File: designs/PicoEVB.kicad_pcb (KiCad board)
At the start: 4 copper layers, 34.3 x 8.4 mm, 109 parts, among them J1 Bus_PCI_Express_x4, J10 1P2, J11 1P0, J12 GND, J2 2.54mm Through-Hole Socket, J3 2.54mm Through-Hole Socket, J7 3P3, J8 1P8, J9 1P0, P2 USB_C_Plug_USB2.0, U1A1 XC7AxxT-xCSG325, U2 S25Q, U3 TPS82085SIL, U4 MAX1589AETT100T, U5 MIC47050-1.2YML, U6 TPS82085SIL, U7 FT230XQ

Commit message: Add files via upload
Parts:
- C1, C10, C11, C12, C13, C14, C15, C16, C17, C18, C19, C2, C20, C21, C22, C23, C24, C25, C26, C3, C4, C5, C52, C53, C54, C55, C56, C57, C58, C59, C6, C60, C61, C62, C63, C64, C65, C66, C7, C8, C9, J10, J11, J12, J7, J8, J9, L1, R2, R3, R4, R5, U3, U4, U5, U6: moved to B.Cu
- moved C8 74.5 mm to (217.0, 102.0), turned to -90 degrees
- moved C5 74.5 mm to (216.0, 102.0), turned to -90 degrees
- moved C15 74.0 mm to (218.0, 102.0), turned to -90 degrees
- moved J11 72.9 mm to (216.0, 98.5), turned to -90 degrees
- moved C1 72.7 mm to (211.5, 106.0), turned to 90 degrees
- moved C7 71.9 mm to (221.5, 99.7), turned to 90 degrees
- moved J12 71.8 mm to (216.0, 109.5), turned to 90 degrees
- moved J7 71.6 mm to (216.0, 105.0), turned to 90 degrees
- moved C12 71.1 mm to (222.0, 99.7), turned to 90 degrees
- moved C17 70.4 mm to (222.5, 99.7), turned to 90 degrees
- moved C3 68.4 mm to (220.0, 98.5), turned to 90 degrees
- moved C26 68.1 mm to (221.5, 101.5), turned to -90 degrees
- moved C18 67.9 mm to (219.0, 101.5), turned to -90 degrees
- moved C55 67.5 mm to (216.1, 115.0), turned to -90 degrees
- moved C20 67.4 mm to (219.5, 101.5), turned to -90 degrees
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- renumbered U1A1 to U1
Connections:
- C52 pad 1: VCC_BANK14_B -> +3V3
- C53 pad 1: VCC_BANK14_B -> +3V3
- C54 pad 1: VCC_BANK14_B -> +3V3
- C55 pad 1: VCC_BANK14_B -> +3V3
- C58 pad 1: VCC_BANK14_B -> +3V3
- C59 pad 1: VCC_BANK14_B -> +3V3
- C67 pad 1: VCC_BANK14_B -> +3V3
- C68 pad 1: VCC_BANK14_B -> +3V3
- C69 pad 1: VCC_BANK14_B -> +3V3
- C70 pad 2: VCC_BANK14_B -> +3V3
- J1 pad A10: VCC_BANK14_B -> +3V3
- J1 pad A2: unconnected-(J1-+12V-PadA2)_4 -> +3V3
- J1 pad A3: unconnected-(J1-+12V-PadA2)_2 -> +3V3
- J1 pad A9: VCC_BANK14_B -> +3V3
- J1 pad B1: unconnected-(J1-+12V-PadA2)_3 -> +3V3
- J1 pad B10: unconnected-(J1-3.3Vaux-PadB10) -> +3V3
- J1 pad B2: unconnected-(J1-+12V-PadA2) -> +3V3
- J1 pad B3: unconnected-(J1-+12V-PadA2)_1 -> +3V3
- J1 pad B8: VCC_BANK14_B -> +3V3
- J2 pad 1: VCC_BANK14_B -> +3V3
- J2 pad 39: VCC_BANK14_B -> +3V3
- J3 pad 1: VCC_BANK14_B -> +3V3
- J3 pad 39: VCC_BANK14_B -> +3V3
- J7 pad 1: VCC_BANK14_B -> +3V3
- R1 pad 1: Net-(U1E1E-MGTRREF_216) -> Net-(U1E-MGTRREF_216)
- U1 pad A1: (no net) -> GND
- U1 pad A10: (no net) -> XADC_2_N
- U1 pad A11: (no net) -> GND
- U1 pad A12: (no net) -> XADC_3_N
- U1 pad A13: (no net) -> unconnected-(U1C-IO_L8P_T1_AD10P_15-PadA13)
- U1 pad A14: (no net) -> unconnected-(U1C-IO_L8N_T1_AD10N_15-PadA14)
- U1 pad A15: (no net) -> unconnected-(U1C-IO_L10N_T1_AD11N_15-PadA15)
- U1 pad A16: (no net) -> VCC_BANK14_B
- U1 pad A17: (no net) -> unconnected-(U1C-IO_L15N_T2_DQS_ADV_B_15-PadA17)
- U1 pad A18: (no net) -> GND
- U1 pad A2: (no net) -> P1V2_MGTAVTT_B
- U1 pad A3: (no net) -> GND
- U1 pad A4: (no net) -> GND
- U1 pad A5: (no net) -> GND
- U1 pad A6: (no net) -> Net-(U1E-MGTRREF_216)
- U1 pad A7: (no net) -> GND
- U1 pad A8: (no net) -> GND
- U1 pad A9: (no net) -> unconnected-(U1C-IO_L3N_T0_DQS_AD1N_15-PadA9)
- U1 pad B1: (no net) -> MGT0_TX_B-
- U1 pad B10: (no net) -> XADC_2_P
- U1 pad B11: (no net) -> DIO_0_N
- U1 pad B12: (no net) -> XADC_3_P
- U1 pad B13: (no net) -> VCC_BANK14_B
- U1 pad B14: (no net) -> unconnected-(U1C-IO_L10P_T1_AD11P_15-PadB14)
- U1 pad B15: (no net) -> unconnected-(U1C-IO_L9N_T1_DQS_AD3N_15-PadB15)
- U1 pad B16: (no net) -> unconnected-(U1C-IO_L15P_T2_DQS_15-PadB16)
- U1 pad B17: (no net) -> DIO_1_N
- U1 pad B18: (no net) -> GND
- U1 pad B2: (no net) -> MGT0_TX_B+
- U1 pad B3: (no net) -> GND
- U1 pad B4: (no net) -> P1V0_MGTAVCC_B
- U1 pad B5: (no net) -> MGT_REFCLK0_B-
- U1 pad B6: (no net) -> MGT_REFCLK0_B+
- U1 pad B7: (no net) -> GND
- U1 pad B8: (no net) -> GND
- U1 pad B9: (no net) -> unconnected-(U1C-IO_L3P_T0_DQS_AD1P_15-PadB9)
- U1 pad C1: (no net) -> P1V2_MGTAVTT_B
- U1 pad C10: (no net) -> VCC_BANK14_B
- U1 pad C11: (no net) -> DIO_0_P
- U1 pad C12: (no net) -> unconnected-(U1C-IO_L6N_T0_VREF_15-PadC12)
- U1 pad C13: (no net) -> unconnected-(U1C-IO_L11N_T1_SRCC_15-PadC13)
- U1 pad C14: (no net) -> unconnected-(U1C-IO_L9P_T1_DQS_AD3P_15-PadC14)
- U1 pad C15: (no net) -> GND
- U1 pad C16: (no net) -> DIO_1_P
- U1 pad C17: (no net) -> DIO_3_P
- U1 pad C18: (no net) -> DIO_3_N
- U1 pad C2: (no net) -> GND
- U1 pad C3: (no net) -> Net-(U1E-MGTPRXN2_216)
- U1 pad C4: (no net) -> Net-(U1E-MGTPRXP2_216)
- U1 pad C5: (no net) -> P1V0_MGTAVCC_B
- U1 pad C6: (no net) -> GND
- U1 pad C7: (no net) -> GND
- U1 pad C8: (no net) -> XADC_0_N
- U1 pad C9: (no net) -> XADC_1_N
- U1 pad D1: (no net) -> Net-(U1E-MGTPRXN2_216)
- U1 pad D10: (no net) -> GPIO_0
- U1 pad D11: (no net) -> unconnected-(U1C-IO_L6P_T0_15-PadD11)
- U1 pad D12: (no net) -> GND
- U1 pad D13: (no net) -> unconnected-(U1C-IO_L11P_T1_SRCC_15-PadD13)
- U1 pad D14: (no net) -> MRCC_Out_1
- U1 pad D15: (no net) -> MRCC_Out_3
- U1 pad D16: (no net) -> unconnected-(U1C-IO_L14N_T2_SRCC_15-PadD16)
- U1 pad D17: (no net) -> VCC_BANK14_B
- U1 pad D18: (no net) -> DIO_2_N
- U1 pad D2: (no net) -> Net-(U1E-MGTPRXP2_216)
- U1 pad D3: (no net) -> GND
- U1 pad D4: (no net) -> GND
- U1 pad D5: (no net) -> /FPGA PCIe/UMGTCLK_0-
- U1 pad D6: (no net) -> /FPGA PCIe/UMGTCLK_0+
- U1 pad D7: (no net) -> GND
- U1 pad D8: (no net) -> XADC_0_P
- U1 pad D9: (no net) -> XADC_1_P
- U1 pad E1: (no net) -> P1V2_MGTAVTT_B
- U1 pad E13: (no net) -> MRCC_Out_0
- U1 pad E14: (no net) -> VCC_BANK14_B
- U1 pad E15: (no net) -> MRCC_Out_2
- U1 pad E16: (no net) -> unconnected-(U1C-IO_L14P_T2_SRCC_15-PadE16)
- U1 pad E17: (no net) -> DIO_2_P
- U1 pad E18: (no net) -> DIO_7_N
- U1 pad E2: (no net) -> GND
- U1 pad E3: (no net) -> MGT1_RX_B-
- U1 pad E4: (no net) -> MGT1_RX_B+
- U1 pad E5: (no net) -> P1V0_MGTAVCC_B
- U1 pad E6: (no net) -> GND
- U1 pad E7: (no net) -> GND
- U1 pad E9: (no net) -> GND
- U1 pad F1: (no net) -> unconnected-(U1E-MGTPTXN1_216-PadF1)
- U1 pad F10: (no net) -> GND
- U1 pad F11: (no net) -> P1V0_VCC_FPGA_B
- U1 pad F14: (no net) -> DIO_5_N
- U1 pad F15: (no net) -> unconnected-(U1C-IO_L21N_T3_DQS_A18_15-PadF15)
- U1 pad F16: (no net) -> GND
- U1 pad F17: (no net) -> DIO_7_P
- U1 pad F18: (no net) -> unconnected-(U1C-IO_L19N_T3_A21_VREF_15-PadF18)
- U1 pad F2: (no net) -> unconnected-(U1E-MGTPTXP1_216-PadF2)
- U1 pad F3: (no net) -> P1V2_MGTAVTT_B
- U1 pad F4: (no net) -> GND
- U1 pad F5: (no net) -> P1V0_MGTAVCC_B
- U1 pad F6: (no net) -> GND
- U1 pad F7: (no net) -> P1V0_VCC_FPGA_B
- U1 pad F9: (no net) -> P1V0_VCC_FPGA_B
- U1 pad G1: (no net) -> GND
- U1 pad G10: (no net) -> P1V0_VCC_FPGA_B
- U1 pad G11: (no net) -> GND
- U1 pad G12: (no net) -> P1V8_FPGA_VCCAUX_B
- U1 pad G13: (no net) -> GND
- U1 pad G14: (no net) -> DIO_5_P
- U1 pad G15: (no net) -> unconnected-(U1C-IO_L21P_T3_DQS_15-PadG15)
- U1 pad G16: (no net) -> DIO_4_N
- U1 pad G17: (no net) -> unconnected-(U1C-IO_L19P_T3_A22_15-PadG17)
- U1 pad G18: (no net) -> VCC_BANK14_B
- U1 pad G2: (no net) -> P1V2_MGTAVTT_B
- U1 pad G3: (no net) -> MGT0_RX_B-
- U1 pad G4: (no net) -> MGT0_RX_B+
- U1 pad G5: (no net) -> GND
- U1 pad G6: (no net) -> GND
- U1 pad G7: (no net) -> GND
- U1 pad G8: (no net) -> P1V0_VCC_FPGA_B
- U1 pad G9: (no net) -> GND
- U1 pad H1: (no net) -> MGT1_TX_B-
- U1 pad H10: (no net) -> GND
- U1 pad H11: (no net) -> P1V0_VCC_FPGA_B
- U1 pad H12: (no net) -> GND
- U1 pad H13: (no net) -> P1V8_FPGA_VCCAUX_B
- U1 pad H14: (no net) -> GPIO_1
- U1 pad H15: (no net) -> VCC_BANK14_B
- U1 pad H16: (no net) -> DIO_4_P
- U1 pad H17: (no net) -> DIO_6_P
- U1 pad H18: (no net) -> DIO_6_N
- U1 pad H2: (no net) -> MGT1_TX_B+
- U1 pad H3: (no net) -> GND
- U1 pad H4: (no net) -> GND
- U1 pad H5: (no net) -> GND
- U1 pad H6: (no net) -> GND
- U1 pad H7: (no net) -> P1V0_VCC_FPGA_B
- U1 pad H8: (no net) -> GND
- U1 pad H9: (no net) -> P1V0_VCC_FPGA_B
- U1 pad J1: (no net) -> GND
- U1 pad J11: (no net) -> GND
- U1 pad J12: (no net) -> P1V0_VCC_FPGA_B
- U1 pad J13: (no net) -> GND
- U1 pad J14: (no net) -> unconnected-(U1B-IO_L5P_T0_D06_14-PadJ14)
- U1 pad J15: (no net) -> Net-(RN3-R3.2)
- U1 pad J16: (no net) -> Net-(RN3-R2.2)
- U1 pad J17: (no net) -> GND
- U1 pad J18: (no net) -> VCC_BANK14_B
- U1 pad J2: (no net) -> GND
- U1 pad J3: (no net) -> GND
- U1 pad J4: (no net) -> DIO_9_N
- U1 pad J5: (no net) -> DIO_9_P
- U1 pad J6: (no net) -> GPIO_2
- U1 pad J7: (no net) -> GND
- U1 pad J8: (no net) -> P1V0_VCC_FPGA_B
- U1 pad K1: (no net) -> unconnected-(U1D-IO_L3N_T0_DQS_34-PadK1)
- U1 pad K11: (no net) -> P1V0_VCC_FPGA_B
- U1 pad K12: (no net) -> GND
- U1 pad K13: (no net) -> P1V8_FPGA_VCCAUX_B
- U1 pad K14: (no net) -> GND
- U1 pad K15: (no net) -> unconnected-(U1B-IO_L5N_T0_D07_14-PadK15)
- U1 pad K16: (no net) -> Net-(U1B-IO_L1P_T0_D00_MOSI_14)
- U1 pad K17: (no net) -> unconnected-(U1B-IO_L4P_T0_D04_14-PadK17)
- U1 pad K18: (no net) -> unconnected-(U1B-IO_L3N_T0_DQS_EMCCLK_14-PadK18)
- U1 pad K2: (no net) -> unconnected-(U1D-IO_L3P_T0_DQS_34-PadK2)
- U1 pad K3: (no net) -> DIO_10_P
- U1 pad K4: (no net) -> GND
- U1 pad K5: (no net) -> DIO_8_N
- U1 pad K6: (no net) -> DIO_8_P
- U1 pad K7: (no net) -> P1V0_VCC_FPGA_B
- U1 pad K8: (no net) -> GND
- U1 pad L1: (no net) -> GND
- U1 pad L11: (no net) -> GND
- U1 pad L12: (no net) -> P1V0_VCC_FPGA_B
- U1 pad L13: (no net) -> GND
- U1 pad L14: (no net) -> GPIO_4
- U1 pad L15: (no net) -> Net-(RN3-R4.2)
- U1 pad L16: (no net) -> VCC_BANK14_B
- U1 pad L17: (no net) -> Net-(U1B-IO_L1N_T0_D01_DIN_14)
- U1 pad L18: (no net) -> unconnected-(U1B-IO_L4N_T0_D05_14-PadL18)
- U1 pad L2: (no net) -> DIO_10_N
- U1 pad L3: (no net) -> DIO_11_N
- U1 pad L4: (no net) -> DIO_11_P
- U1 pad L5: (no net) -> unconnected-(U1D-IO_L6P_T0_34-PadL5)
- U1 pad L6: (no net) -> VCC_BANK14_B
- U1 pad L7: (no net) -> GND
- U1 pad L8: (no net) -> P1V0_VCC_FPGA_B
- U1 pad M1: (no net) -> DIO_12_N
- U1 pad M11: (no net) -> P1V0_VCC_FPGA_B
- U1 pad M12: (no net) -> GND
- U1 pad M13: (no net) -> P1V8_FPGA_VCCAUX_B
- U1 pad M14: (no net) -> unconnected-(U1B-IO_L8P_T1_D11_14-PadM14)
- U1 pad M15: (no net) -> unconnected-(U1B-IO_L6N_T0_D08_VREF_14-PadM15)
- U1 pad M16: (no net) -> unconnected-(U1B-IO_L7P_T1_D09_14-PadM16)
- U1 pad M17: (no net) -> unconnected-(U1B-IO_L7N_T1_D10_14-PadM17)
- U1 pad M18: (no net) -> GND
- U1 pad M2: (no net) -> DIO_12_P
- U1 pad M3: (no net) -> VCC_BANK14_B
- U1 pad M4: (no net) -> DIO_14_P
- U1 pad M5: (no net) -> unconnected-(U1D-IO_L6N_T0_VREF_34-PadM5)
- U1 pad M6: (no net) -> DIO_13_P
- U1 pad M7: (no net) -> P1V0_VCC_FPGA_B
- U1 pad M8: (no net) -> GND
- U1 pad N1: (no net) -> unconnected-(U1D-IO_L9P_T1_DQS_34-PadN1)
- U1 pad N10: (no net) -> P1V0_VCC_FPGA_B
- U1 pad N11: (no net) -> GND
- U1 pad N12: (no net) -> P1V0_VCC_FPGA_B
- U1 pad N13: (no net) -> GND
- U1 pad N14: (no net) -> unconnected-(U1B-IO_L8N_T1_D12_14-PadN14)
- U1 pad N15: (no net) -> GND
- U1 pad N16: (no net) -> unconnected-(U1B-IO_L9P_T1_DQS_14-PadN16)
- U1 pad N17: (no net) -> unconnected-(U1B-IO_L9N_T1_DQS_D13_14-PadN17)
- U1 pad N18: (no net) -> unconnected-(U1B-IO_L10P_T1_D14_14-PadN18)
- U1 pad N2: (no net) -> unconnected-(U1D-IO_L11N_T1_SRCC_34-PadN2)
- U1 pad N3: (no net) -> unconnected-(U1D-IO_L11P_T1_SRCC_34-PadN3)
- U1 pad N4: (no net) -> DIO_14_N
- U1 pad N5: (no net) -> GND
- U1 pad N6: (no net) -> DIO_13_N
- U1 pad N7: (no net) -> GND
- U1 pad N8: (no net) -> P1V0_VCC_FPGA_B
- U1 pad N9: (no net) -> GND
- U1 pad P1: (no net) -> unconnected-(U1D-IO_L9N_T1_DQS_34-PadP1)
- U1 pad P11: (no net) -> P1V0_VCC_FPGA_B
- U1 pad P12: (no net) -> GND
- U1 pad P13: (no net) -> P1V8_FPGA_VCCAUX_B
- U1 pad P14: (no net) -> unconnected-(U1B-IO_L12P_T1_MRCC_14-PadP14)
- U1 pad P15: (no net) -> unconnected-(U1B-IO_L11P_T1_SRCC_14-PadP15)
- U1 pad P16: (no net) -> unconnected-(U1B-IO_L11N_T1_SRCC_14-PadP16)
- U1 pad P17: (no net) -> VCC_BANK14_B
- U1 pad P18: (no net) -> unconnected-(U1B-IO_L10N_T1_D15_14-PadP18)
- U1 pad P2: (no net) -> GND
- U1 pad P3: (no net) -> unconnected-(U1D-IO_L12N_T1_MRCC_34-PadP3)
- U1 pad P4: (no net) -> unconnected-(U1D-IO_L12P_T1_MRCC_34-PadP4)
- U1 pad P5: (no net) -> unconnected-(U1D-IO_L19N_T3_VREF_34-PadP5)
- U1 pad P6: (no net) -> unconnected-(U1D-IO_L19P_T3_34-PadP6)
- U1 pad P7: (no net) -> VCC_BANK14_B
- U1 pad P8: (no net) -> GND
- U1 pad P9: (no net) -> P1V0_VCC_FPGA_B
- U1 pad R1: (no net) -> unconnected-(U1D-IO_L13N_T2_MRCC_34-PadR1)
- U1 pad R13: (no net) -> unconnected-(U1B-IO_L19P_T3_A10_D26_14-PadR13)
- U1 pad R14: (no net) -> VCC_BANK14_B
- U1 pad R15: (no net) -> unconnected-(U1B-IO_L12N_T1_MRCC_14-PadR15)
- U1 pad R16: (no net) -> unconnected-(U1B-IO_L14P_T2_SRCC_14-PadR16)
- U1 pad R17: (no net) -> unconnected-(U1B-IO_L14N_T2_SRCC_14-PadR17)
- U1 pad R18: (no net) -> unconnected-(U1B-IO_L15P_T2_DQS_RDWR_B_14-PadR18)
- U1 pad R2: (no net) -> unconnected-(U1D-IO_L13P_T2_MRCC_34-PadR2)
- U1 pad R3: (no net) -> unconnected-(U1D-IO_L14P_T2_SRCC_34-PadR3)
- U1 pad R4: (no net) -> VCC_BANK14_B
- U1 pad R5: (no net) -> unconnected-(U1D-IO_L21P_T3_DQS_34-PadR5)
- U1 pad R6: (no net) -> GPIO_3
- U1 pad R7: (no net) -> unconnected-(U1D-IO_L22P_T3_34-PadR7)
- U1 pad R9: (no net) -> GND
- U1 pad T1: (no net) -> VCC_BANK14_B
- U1 pad T11: (no net) -> VCC_BANK14_B
- U1 pad T12: (no net) -> unconnected-(U1B-IO_L22P_T3_A05_D21_14-PadT12)
- U1 pad T13: (no net) -> unconnected-(U1B-IO_L19N_T3_A09_D25_VREF_14-PadT13)
- U1 pad T14: (no net) -> unconnected-(U1B-IO_L13P_T2_MRCC_14-PadT14)
- U1 pad T15: (no net) -> unconnected-(U1B-IO_L13N_T2_MRCC_14-PadT15)
- U1 pad T16: (no net) -> GND
- U1 pad T17: (no net) -> unconnected-(U1B-IO_L16P_T2_CSI_B_14-PadT17)
- U1 pad T18: (no net) -> unconnected-(U1B-IO_L15N_T2_DQS_DOUT_CSO_B_14-PadT18)
- U1 pad T2: (no net) -> unconnected-(U1D-IO_L14N_T2_SRCC_34-PadT2)
- U1 pad T3: (no net) -> DIO_15_N
- U1 pad T4: (no net) -> DIO_15_P
- U1 pad T5: (no net) -> unconnected-(U1D-IO_L21N_T3_DQS_34-PadT5)
- U1 pad T6: (no net) -> GND
- U1 pad T7: (no net) -> unconnected-(U1D-IO_L22N_T3_34-PadT7)
- U1 pad U1: (no net) -> unconnected-(U1D-IO_L15N_T2_DQS_34-PadU1)
- U1 pad U10: (no net) -> GPIO_5
- U1 pad U11: (no net) -> unconnected-(U1B-IO_L23P_T3_A03_D19_14-PadU11)
- U1 pad U12: (no net) -> unconnected-(U1B-IO_L22N_T3_A04_D20_14-PadU12)
- U1 pad U13: (no net) -> GND
- U1 pad U14: (no net) -> unconnected-(U1B-IO_L20P_T3_A08_D24_14-PadU14)
- U1 pad U15: (no net) -> unconnected-(U1B-IO_L17P_T2_A14_D30_14-PadU15)
- U1 pad U16: (no net) -> unconnected-(U1B-IO_L17N_T2_A13_D29_14-PadU16)
- U1 pad U17: (no net) -> unconnected-(U1B-IO_L16N_T2_A15_D31_14-PadU17)
- U1 pad U18: (no net) -> VCC_BANK14_B
- U1 pad U2: (no net) -> unconnected-(U1D-IO_L15P_T2_DQS_34-PadU2)
- U1 pad U3: (no net) -> GND
- U1 pad U4: (no net) -> DIO_16_P
- U1 pad U5: (no net) -> unconnected-(U1D-IO_L20N_T3_34-PadU5)
- U1 pad U6: (no net) -> unconnected-(U1D-IO_L20P_T3_34-PadU6)
- U1 pad U7: (no net) -> unconnected-(U1D-IO_L23P_T3_34-PadU7)
- U1 pad U8: (no net) -> VCC_BANK14_B
- U1 pad U9: (no net) -> unconnected-(U1B-IO_L24P_T3_A01_D17_14-PadU9)
- U1 pad V1: (no net) -> GND
- U1 pad V10: (no net) -> GND
- U1 pad V11: (no net) -> unconnected-(U1B-IO_L23N_T3_A02_D18_14-PadV11)
- U1 pad V12: (no net) -> Net-(D3-K)
- U1 pad V13: (no net) -> Net-(D4-K)
- U1 pad V14: (no net) -> Net-(D2-K)
- U1 pad V15: (no net) -> VCC_BANK14_B
- U1 pad V16: (no net) -> unconnected-(U1B-IO_L18P_T2_A12_D28_14-PadV16)
- U1 pad V17: (no net) -> unconnected-(U1B-IO_L18N_T2_A11_D27_14-PadV17)
- U1 pad V18: (no net) -> GND
- U1 pad V2: (no net) -> M2_LED_1
- U1 pad V3: (no net) -> M2_LED_2
- U1 pad V4: (no net) -> DIO_16_N
- U1 pad V5: (no net) -> VCC_BANK14_B
- U1 pad V6: (no net) -> unconnected-(U1D-IO_L23N_T3_34-PadV6)
- U1 pad V7: (no net) -> unconnected-(U1D-IO_L24N_T3_34-PadV7)
- U1 pad V8: (no net) -> unconnected-(U1D-IO_L24P_T3_34-PadV8)
- U1 pad V9: (no net) -> unconnected-(U1B-IO_L24N_T3_A00_D16_14-PadV9)
- U2 pad 2: Net-(U1B1B-IO_L1N_T0_D01_DIN_14) -> Net-(U1B-IO_L1N_T0_D01_DIN_14)
- U2 pad 5: Net-(U1B1B-IO_L1P_T0_D00_MOSI_14) -> Net-(U1B-IO_L1P_T0_D00_MOSI_14)
- U3 pad 1: VCC_BANK14_B -> +3V3
- U3 pad 3: VCC_BANK14_B -> +3V3
- U3 pad 4: VCC_BANK14_B -> +3V3
- U5 pad 1: VCC_BANK14_B -> +3V3
- U5 pad 6: VCC_BANK14_B -> +3V3
- U6 pad 1: VCC_BANK14_B -> +3V3
- U6 pad 3: VCC_BANK14_B -> +3V3
- U6 pad 4: VCC_BANK14_B -> +3V3
- U7 pad 1: VCC_BANK14_B -> +3V3
- U7 pad 10: VCC_BANK14_B -> +3V3
- U7 pad 8: VCC_BANK14_B -> +3V3
- U7 pad 9: VCC_BANK14_B -> Net-(U7-~{RESET})
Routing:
- net GND: track 0.00 -> 128.5 mm, vias 0 -> 60
- net +3V3: track 0.00 -> 51.7 mm, vias 0 -> 17
- net P1V0_VCC_FPGA_B: track 0.00 -> 41.6 mm, vias 0 -> 1
- net P1V8_FPGA_VCCAUX_B: track 0.00 -> 22.4 mm
- net P1V2_MGTAVTT_B: track 0.00 -> 18.1 mm, vias 0 -> 1
- net Net-(U3-VOUT): track 0.00 -> 17.8 mm
- net P1V0_MGTAVCC_B: track 0.00 -> 16.8 mm, vias 0 -> 1
- net Net-(U6-FB): track 0.00 -> 2.71 mm
- net Net-(U3-FB): track 0.00 -> 1.55 mm
- added copper zone on In2.Cu, net +3V3
- added copper zone on In1.Cu, net GND
- added copper zone on In3.Cu, net GND
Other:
- copper layers 4 -> 6

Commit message: Add changes
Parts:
- added ?: , , F.Cu at (193.3, 66.7)
- added C13: 0.1uf, SMT:c_0201_least, B.Cu at (205.7, 55.2)
- added C14: 0.1uf, SMT:c_0201_least, B.Cu at (193.5, 67.3)
- added C14: 0.1uf, SMT:c_0201_least, B.Cu at (193.5, 67.8)
- added C14: 0.1uf, SMT:c_0201_least, B.Cu at (193.5, 66.7)
- added C18: 0.47uf, SMT:c_0201_least, B.Cu at (228.4, 67.6)
- added C18: 0.47uf, SMT:c_0201_least, B.Cu at (225.3, 67.6)
- added C20: 0.47uf, SMT:c_0201_least, B.Cu at (228.9, 67.6)
- added C20: 0.47uf, SMT:c_0201_least, B.Cu at (225.8, 67.6)
- added C21: 0.47uf, SMT:c_0201_least, B.Cu at (199.5, 62.4)
- added C22: 0.47uf, SMT:c_0201_least, B.Cu at (229.4, 67.6)
- added C22: 0.47uf, SMT:c_0201_least, B.Cu at (226.3, 67.6)
- added C23: 0.47uf, SMT:c_0201_least, B.Cu at (200.5, 62.4)
- added C24: 0.47uf, SMT:c_0201_least, B.Cu at (226.8, 67.6)
- added C25: 0.47uf, SMT:c_0201_least, B.Cu at (227.3, 67.6)
- added C26: 0.47uf, SMT:c_0201_least, B.Cu at (227.8, 67.6)
- added C9: 0.1uf, SMT:c_0201_least, B.Cu at (205.6, 56.0)
- moved C1 55.3 mm to (204.0, 51.2)
- moved C9 54.3 mm to (204.8, 52.4)
- moved C13 53.5 mm to (205.6, 53.2)
- moved C11 37.9 mm to (194.4, 62.1)
- moved C16 37.9 mm to (195.4, 62.4)
- moved C19 37.9 mm to (196.4, 62.4)
- moved C21 37.9 mm to (197.4, 62.4)
- moved C23 37.9 mm to (198.4, 62.4)
- moved C4 37.9 mm to (191.9, 61.9)
- moved C6 37.9 mm to (193.4, 62.1)
- moved C12 34.9 mm to (230.3, 65.8)
- moved C17 34.9 mm to (230.8, 65.8)
- moved C7 34.9 mm to (229.8, 65.8)
- moved C15 34.1 mm to (221.2, 68.1)
- moved C18 34.1 mm to (222.2, 67.6)
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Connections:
- U3 pad : (no net) -> GND
- U6 pad : (no net) -> GND
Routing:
- net GND: track 128.5 -> 107.0 mm, vias 60 -> 182
- net Net-(U3-VOUT): track 17.8 -> 6.30 mm
- net P1V0_VCC_FPGA_B: track 41.6 -> 51.8 mm, vias 1 -> 21
- net P1V2_MGTAVTT_B: track 18.1 -> 20.3 mm, vias 1 -> 5
- net P1V8_FPGA_VCCAUX_B: track 22.4 -> 23.7 mm, vias 0 -> 6
- net +3V3: track 51.7 -> 52.3 mm, vias 17 -> 16
- net Net-(U3-FB): track 1.55 -> 2.05 mm
- net P1V0_MGTAVCC_B: track 16.8 -> 16.4 mm, vias 1 -> 4
- net unconnected-(U1E-MGTPTXP1_216-PadF2): vias 0 -> 1
- net unconnected-(U1E-MGTPTXN1_216-PadF1): vias 0 -> 1
- net unconnected-(U1D-IO_L9P_T1_DQS_34-PadN1): vias 0 -> 1
- net unconnected-(U1D-IO_L9N_T1_DQS_34-PadP1): vias 0 -> 1
- net unconnected-(U1D-IO_L6P_T0_34-PadL5): vias 0 -> 1
- net unconnected-(U1D-IO_L6N_T0_VREF_34-PadM5): vias 0 -> 1
- net unconnected-(U1D-IO_L3P_T0_DQS_34-PadK2): vias 0 -> 1
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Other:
- board text added: "0.47uf"
- board text added: "Needs 21 decoupling caps in total, VCCBRAM only 3"
- board text added: "THESE 3 ARE FOR VCCBRAM: F11, G10, H11"

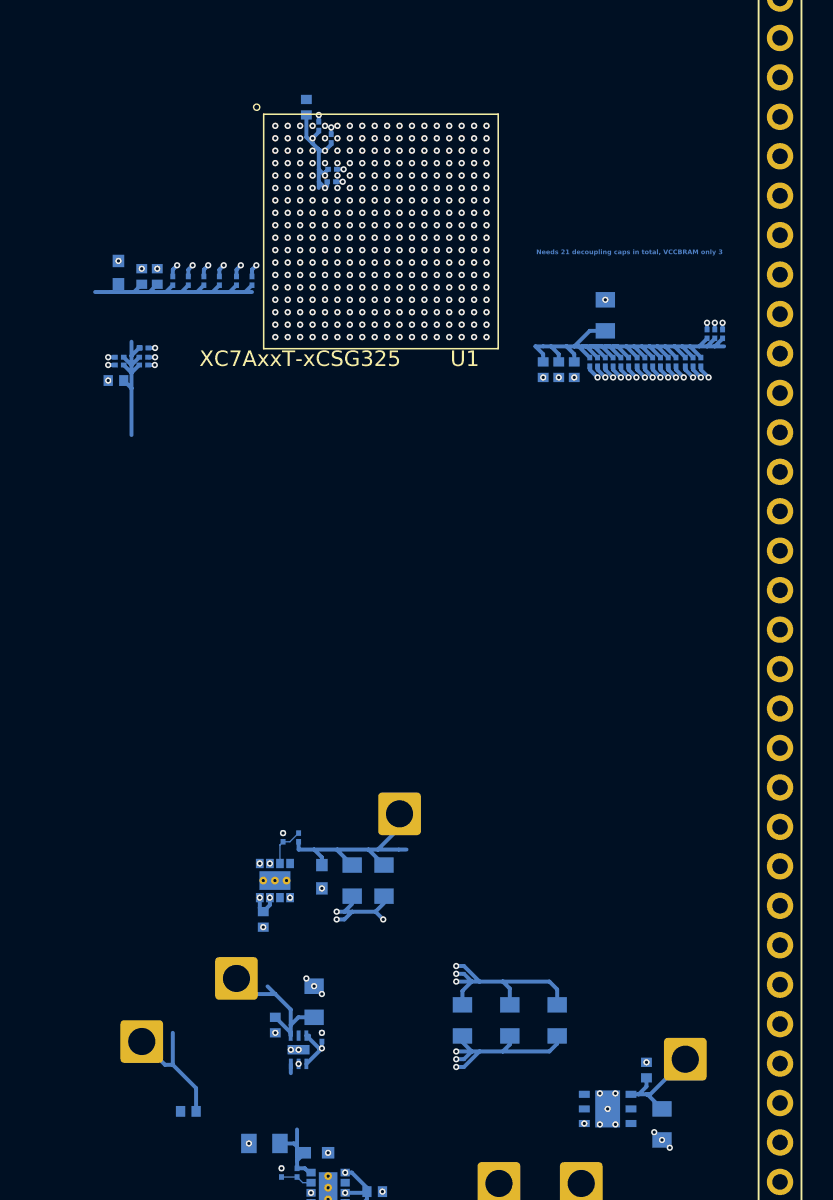
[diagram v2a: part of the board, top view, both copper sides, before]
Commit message: Commit power circuits for chip
All power circuits for chip are DONE. In progress: Connecting bottom of board power circuits.
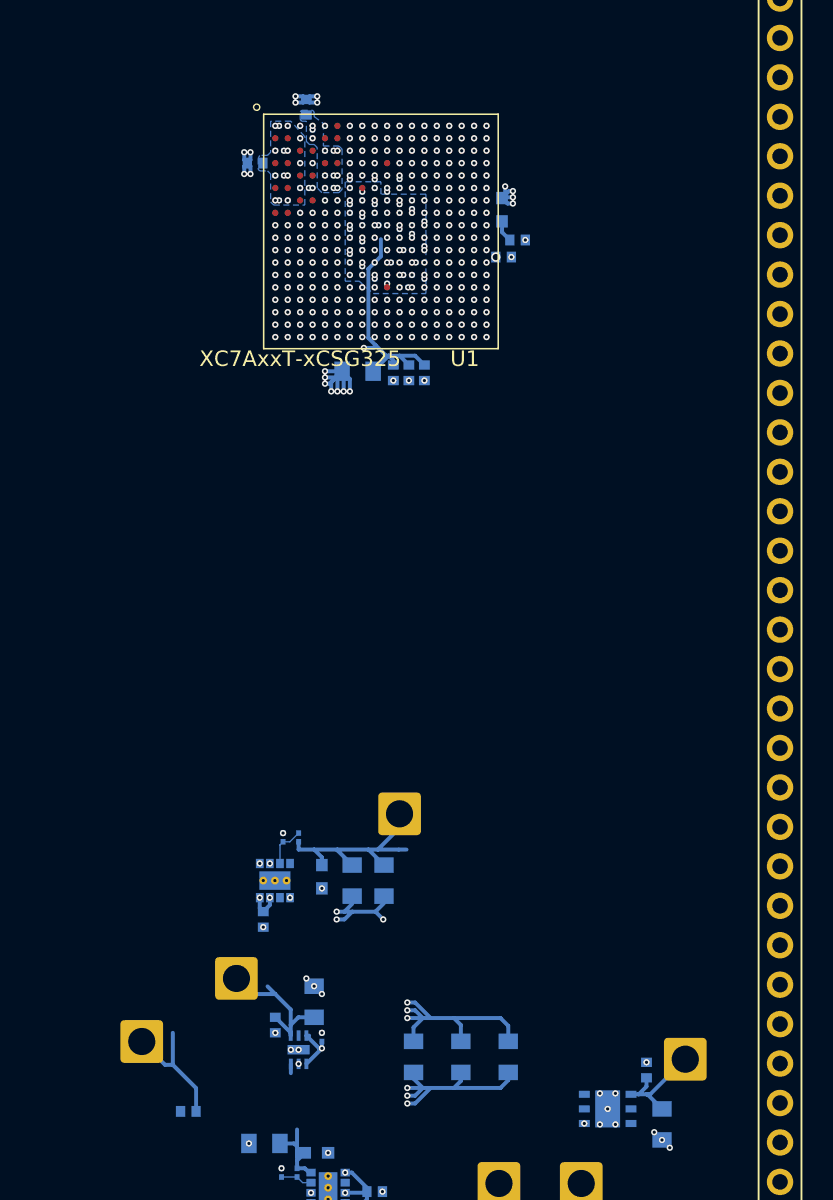
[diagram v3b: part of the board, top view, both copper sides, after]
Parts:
- added C18: 0.47uf, SMT:c_0201_least, B.Cu at (209.2, 62.3)
- added C18: 0.47uf, SMT:c_0201_least, B.Cu at (210.3, 62.8)
- added C18: 0.47uf, SMT:c_0201_least, B.Cu at (210.5, 62.0)
- moved C4 25.0 mm to (216.6, 57.8)
- moved C20 24.9 mm to (206.8, 56.1), turned to 90 degrees
- moved C6 24.3 mm to (217.6, 59.8), turned to 0 degrees
- moved C22 23.9 mm to (208.4, 56.1), turned to 90 degrees
- moved C18 23.4 mm to (207.6, 56.9), turned to 90 degrees
- moved C17 23.4 mm to (209.2, 56.9)
- moved C25 22.8 mm to (206.8, 57.7), turned to 90 degrees
- moved C11 22.3 mm to (216.7, 60.9), turned to 0 degrees
- moved C7 22.0 mm to (210.0, 56.1)
- moved C12 21.8 mm to (210.0, 57.7)
- moved C26 21.8 mm to (208.4, 57.7), turned to 90 degrees
- moved C24 21.2 mm to (207.6, 58.5), turned to 90 degrees
- moved C22 21.2 mm to (206.8, 59.3), turned to 90 degrees
- moved C18 19.2 mm to (207.6, 60.1), turned to 90 degrees
- moved C26 19.2 mm to (206.8, 60.9), turned to 90 degrees
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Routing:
- net P1V0_VCC_FPGA_B: track 51.8 -> 39.3 mm, vias 21 -> 22
- net P1V2_MGTAVTT_B: track 20.3 -> 10.0 mm
- net P1V0_MGTAVCC_B: track 16.4 -> 7.09 mm
- net P1V8_FPGA_VCCAUX_B: track 23.7 -> 14.5 mm, vias 6 -> 7
- net GND: track 107.0 -> 101.7 mm, vias 182 -> 201
- net unconnected-(U1E-MGTPTXP1_216-PadF2): vias 1 -> 0
- net unconnected-(U1E-MGTPTXN1_216-PadF1): vias 1 -> 0
- net Net-(U1E-MGTRREF_216): vias 1 -> 0
- net Net-(U1E-MGTPRXP2_216): vias 2 -> 0
- net Net-(U1E-MGTPRXN2_216): vias 2 -> 0
- net Net-(RN1-R3.2): vias 1 -> 0
- net MGT_REFCLK0_B-: vias 1 -> 0
- net MGT_REFCLK0_B+: vias 1 -> 0
- net MGT1_TX_B-: vias 1 -> 0
- net MGT1_TX_B+: vias 1 -> 0
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- added copper zone on B.Cu, net P1V0_MGTAVCC_B
- added copper zone on B.Cu, net P1V0_VCC_FPGA_B
- added copper zone on In2.Cu, net P1V0_VCC_FPGA_B
- added copper zone on B.Cu, net P1V2_MGTAVTT_B
- added copper zone on In2.Cu, net P1V8_FPGA_VCCAUX_B
- removed copper zone on In2.Cu, net +3V3
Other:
- board text removed: "Needs 21 decoupling caps in total, VCCBRAM only 3"
- board text removed: "THESE 3 ARE FOR VCCBRAM: F11, G10, H11"

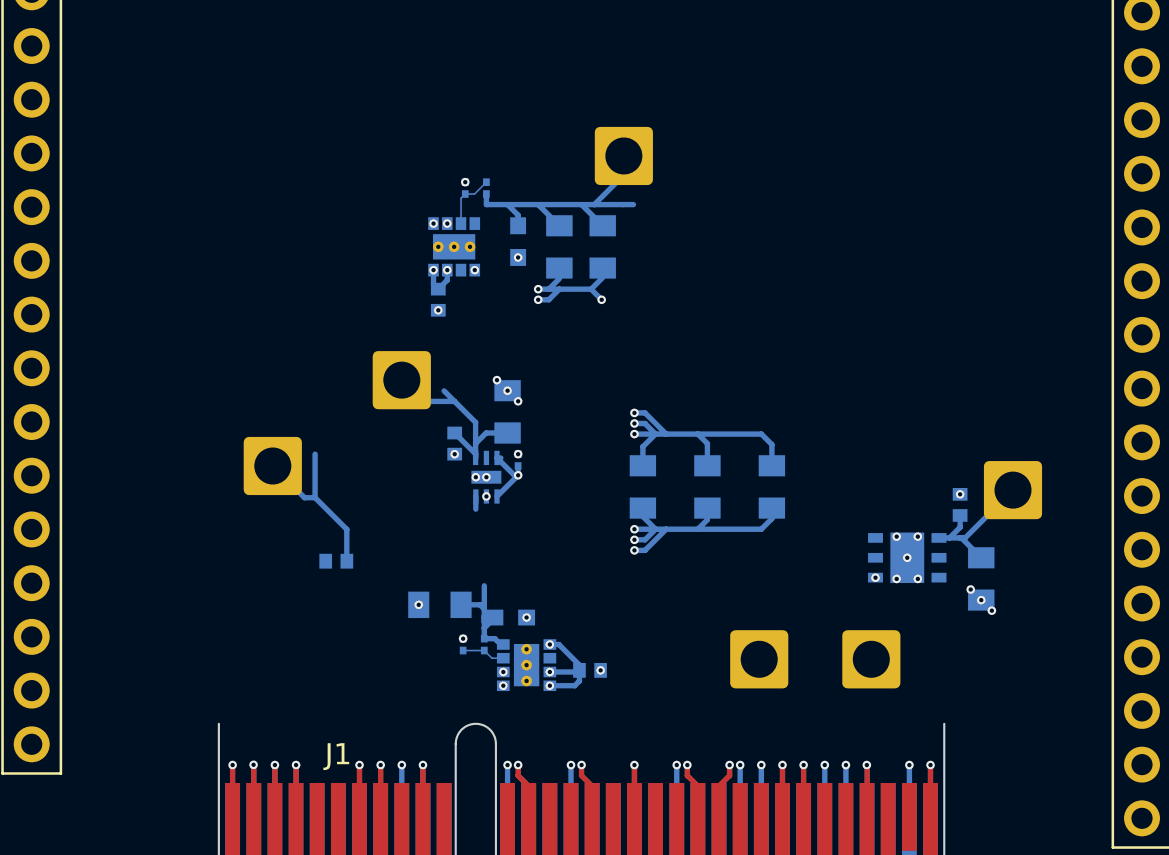
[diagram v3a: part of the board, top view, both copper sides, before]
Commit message: Finished 3V3 filled zone wiring for all ICs
IO yet to be wired.
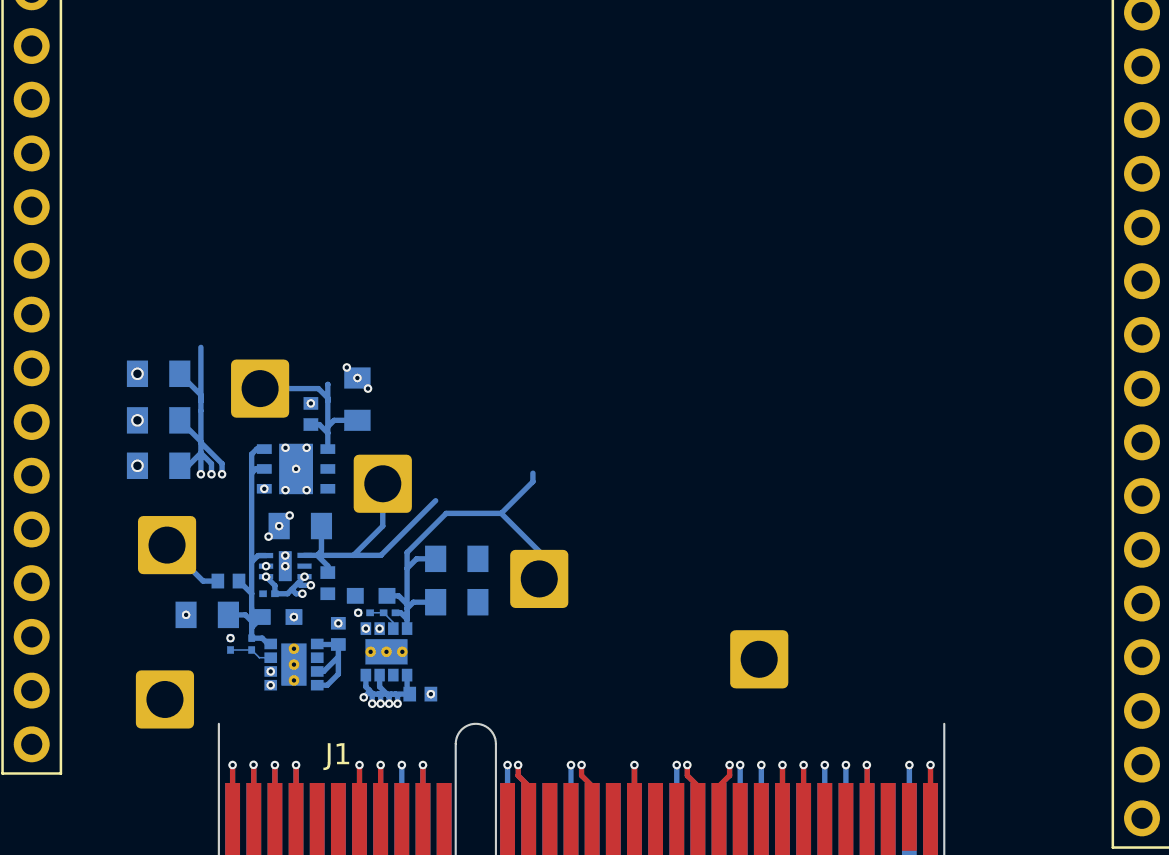
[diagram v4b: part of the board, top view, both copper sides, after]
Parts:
- moved J9 35.9 mm to (192.8, 107.7)
- moved J7 33.5 mm to (188.3, 122.4)
- moved C60 31.0 mm to (195.2, 108.9)
- moved C62 30.7 mm to (197.4, 108.2), turned to 90 degrees
- moved C55 29.5 mm to (188.0, 107.0), turned to 0 degrees
- moved U4 29.2 mm to (194.5, 111.5)
- moved C54 26.1 mm to (188.0, 109.2), turned to 0 degrees
- moved C53 22.9 mm to (188.0, 111.3), turned to 0 degrees
- moved R5 20.6 mm to (197.7, 118.3), turned to 180 degrees
- moved R4 20.6 mm to (198.9, 118.3), turned to 180 degrees
- moved J11 20.4 mm to (206.0, 116.7)
- moved U6 19.4 mm to (198.8, 120.1)
- moved C58 18.7 mm to (200.4, 122.1), turned to 0 degrees
- moved C64 18.1 mm to (198.1, 117.5), turned to 180 degrees
- moved C65 17.5 mm to (202.1, 117.8), turned to 0 degrees
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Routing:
- net +3V3: track 52.3 -> 43.0 mm, vias 16 -> 19
- net Net-(U3-VOUT): track 6.30 -> 15.0 mm
- net P1V0_VCC_FPGA_B: track 39.3 -> 45.1 mm
- net P1V8_FPGA_VCCAUX_B: track 14.5 -> 9.31 mm
- net GND: track 101.7 -> 96.6 mm, vias 201 -> 195
- net P1V2_MGTAVTT_B: track 10.0 -> 13.7 mm
- net P1V0_MGTAVCC_B: track 7.09 -> 9.09 mm
- net Net-(U6-FB): track 2.71 -> 1.58 mm
- added copper zone on In2.Cu, net +3V3
